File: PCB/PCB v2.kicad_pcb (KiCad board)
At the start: 4 copper layers, 56 x 45 mm, 132 parts, among them J2 USB_C_Receptacle_PowerOnly_6P, J3 6871XX182122_687110182122, J5 Conn_01x03_Pin, J7 Conn_02x06_Odd_Even, U1 TPD2E2U06DCK, U11 OPA4350EA_250, U12 OPA4350EA_250, U13 OPA4350EA_250, U2 ADS131M08xPBS, U3 74LVC1G17, U4 LM27762, U6 OPA4350EA_250, U7 LP5907MFX-3.3

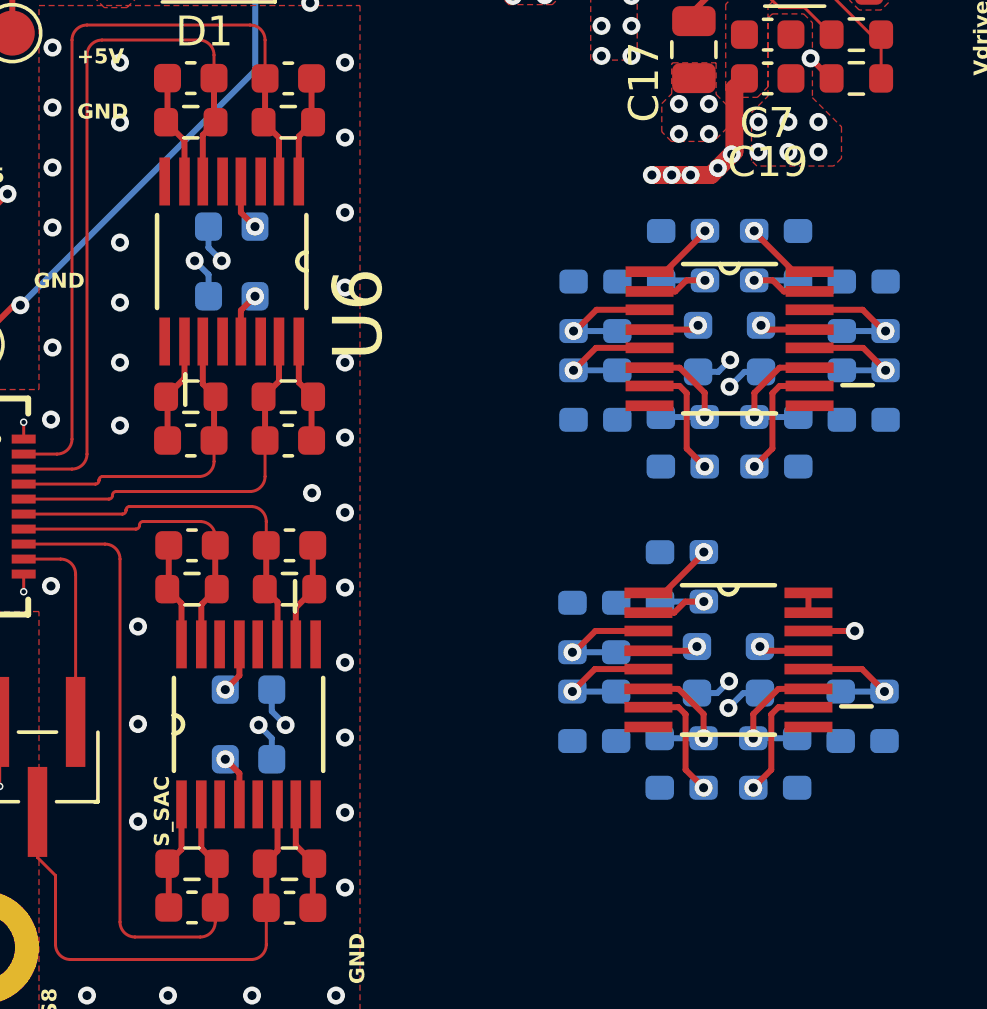
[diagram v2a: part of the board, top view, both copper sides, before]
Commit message: Route charge-amp outputs Q1-Q7 to the difference amplifiers
Each first-stage output Qn feeds its diff-amp input resistor, which sits
on B.Cu under U11 (channels 1-4) or U12 (channels 5-7).

Q1 and Q5-Q7 (routed in pcbnew, 0.1 mm):
- Q1 runs on F.Cu from U6 pin 1 and ends in a via-in-pad at R23.
- Q5-Q7 run from U13 through its centre channel, between the pin rows.
- Q5/Q6/Q7 end in vias at R50/R51/R60.

Q2-Q4 (0.1 mm, same style):
- Q2 and Q3 sit on the left of U6 and are closed off on F.Cu: S1/S2 run
  over the top of U6 and S3/S4 come up from below. So they leave through
  U6's centre channel instead:
  - Q2 at y 94.54, above the two GND vias; Q3 at y 95.68, below them.
  - Guard copper fills between each trace and its pin row, so another
    channel's -IN pin sees only fringing field. Estimated -70 to -90 dB
    crosstalk in band.
  - Q2 then drops at x 139.9 into a via-in-pad at R28 (U11 bottom-left).
  - Q3 drops at x 138.9, runs under U11 at y 103.1 and comes up into a
    via-in-pad at R40 (bottom-right).
- Q4 has to cross Q1 to reach R41 at U11's top-right. It leaves the
  guard on F.Cu, drops through a via at (137.5, 99.64), and runs on B.Cu
  at y 93.0 above U11's top resistor row into R41.
- Every Q net has exactly one via. They are low-impedance op-amp
  outputs at kHz, so the layer change is harmless.
- The guard stitching via at (136.1, 96.0) sat on Q3's exit and moves
  to (136.1, 96.9).

DRC (trial on a snapshot, then re-checked on the saved board):
- Unconnected items 123 -> 120 for Q2-Q4.
- No new clearance, hole or thermal violations.

Co-Authored-By: Claude Opus 5.5 <noreply@anthropic.com>
Claude-Session: https://claude.ai/code/session_01FkMyFfAWNWvsXoQ2tBz5gZ
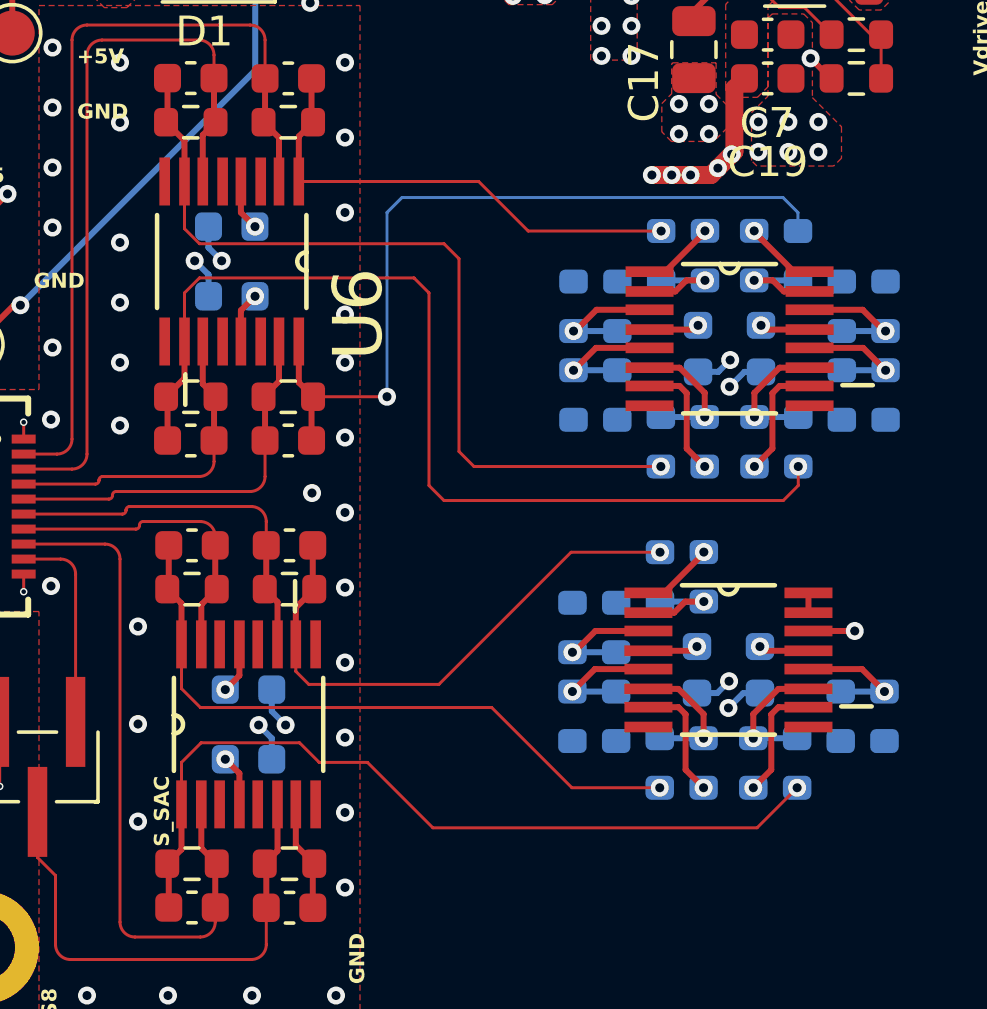
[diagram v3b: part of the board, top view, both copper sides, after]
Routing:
- net /SENSORS/Q3: track 3.58 -> 33.5 mm, vias 0 -> 1
- net /SENSORS/Q2: track 3.72 -> 28.2 mm, vias 0 -> 1
- net /SENSORS/Q7: track 3.65 -> 27.6 mm, vias 0 -> 1
- net /SENSORS/Q4: track 3.52 -> 26.9 mm, vias 0 -> 1
- net /SENSORS/Q6: track 3.52 -> 22.3 mm, vias 0 -> 1
- net /SENSORS/Q5: track 3.58 -> 18.6 mm, vias 0 -> 1
- net /SENSORS/Q1: track 3.65 -> 16.4 mm, vias 0 -> 1
